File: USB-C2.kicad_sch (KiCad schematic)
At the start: 92 parts, among them J4 USB_C_Receptacle, J5 I2C2_PD_Controller, J6 I2C_Mux, J7 I2C_EEPROM, SW2 FW_Upgrade, U10 24LC256, U11 TPD4E02B04DQA, U12 TPD4E02B04DQA, U13 TPD4E02B04DQA, U14 TUSB1142IRNQR_C5216209, U8 TVS2200DRV, U9 TPS25762CQRQLRQ1

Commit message: Schematic reannotated
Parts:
- renumbered C31 to C32, C32 to C33, C33 to C34, C34 to C35, C35 to C36, C36 to C37, C37 to C38, C38 to C39, C39 to C40, C40 to C41, C41 to C42, C42 to C43, C43 to C44, C44 to C45, C45 to C46, C46 to C47, C47 to C48, C48 to C49, C49 to C50, C50 to C51, C51 to C52, C52 to C53, C53 to C54, C54 to C55, C55 to C56, C56 to C57, C57 to C58, C58 to C59, C59 to C60, C60 to C61, C61 to C62, C62 to C63, C63 to C64, C64 to C65, C65 to C66, C66 to C67, C67 to C68, C68 to C69, R12 to R21, R13 to R22, R14 to R23, R15 to R24, R16 to R25, R17 to R26, R18 to R27, R19 to R28, R20 to R29, R21 to R30, R22 to R31, R23 to R32, R24 to R33, R25 to R34, R51 to R35, R52 to R36, R47 to R37, R50 to R38, R26 to R39, R27 to R40, R28 to R41, R29 to R42, R96 to R43, R30 to R44, R31 to R45, R32 to R46, R33 to R47, R34 to R48, R35 to R49, R36 to R50, R37 to R51, R38 to R52, R39 to R53, R40 to R54, R41 to R55, R42 to R56, R43 to R57

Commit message: J11 changed to 8-pin PCIe connector, footprint assigned
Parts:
- J4: footprint Connector_USB:USB_C_Receptacle_Amphenol_12401610E4-2A -> SamacSys_Parts:USB420003A
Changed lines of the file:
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@@
 			)
 		)
-		(property "Footprint" "Connector_USB:USB_C_Receptacle_Amphenol_12401610E4-2A"
+		(property "Footprint" "SamacSys_Parts:USB420003A"
 			(at 374.65 48.26 0)
 			(effects

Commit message: footprints assigned, U21 change to SiRA80DP
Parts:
- TP3, TP4: footprint TestPoint:TestPoint_THTPad_1.5x1.5mm_Drill0.7mm -> TestPoint:TestPoint_Loop_D1.80mm_Drill1.0mm_Beaded
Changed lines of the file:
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@@
 			)
 		)
-		(property "Footprint" "TestPoint:TestPoint_THTPad_1.5x1.5mm_Drill0.7mm"
+		(property "Footprint" "TestPoint:TestPoint_Loop_D1.80mm_Drill1.0mm_Beaded"
 			(at 125.73 113.03 0)
 			(effects
@@
 			)
 		)
-		(property "Footprint" "TestPoint:TestPoint_THTPad_1.5x1.5mm_Drill0.7mm"
+		(property "Footprint" "TestPoint:TestPoint_Loop_D1.80mm_Drill1.0mm_Beaded"
 			(at 300.99 72.39 0)
 			(effects

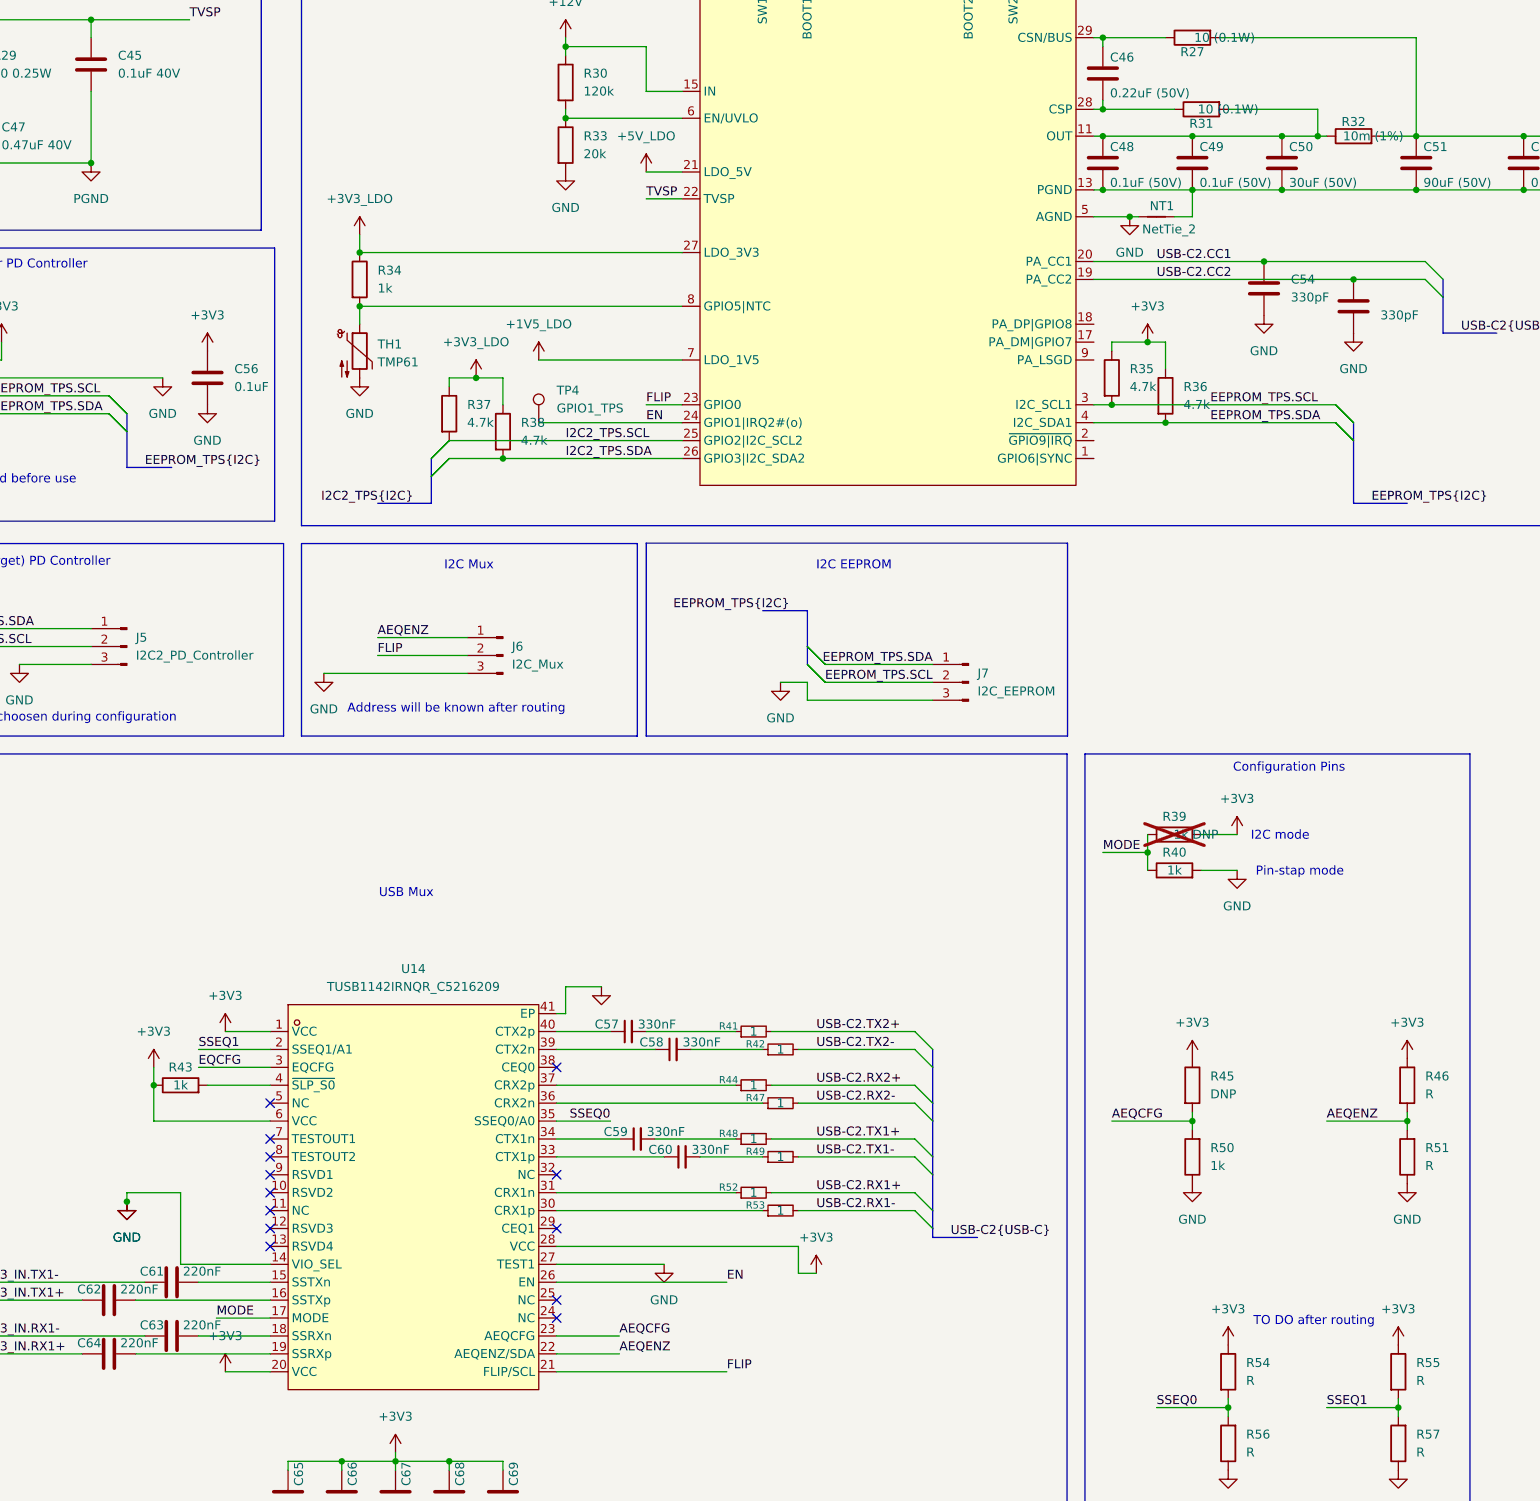
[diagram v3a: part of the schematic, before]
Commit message: Net class for USB SS signals created and applied on schematic
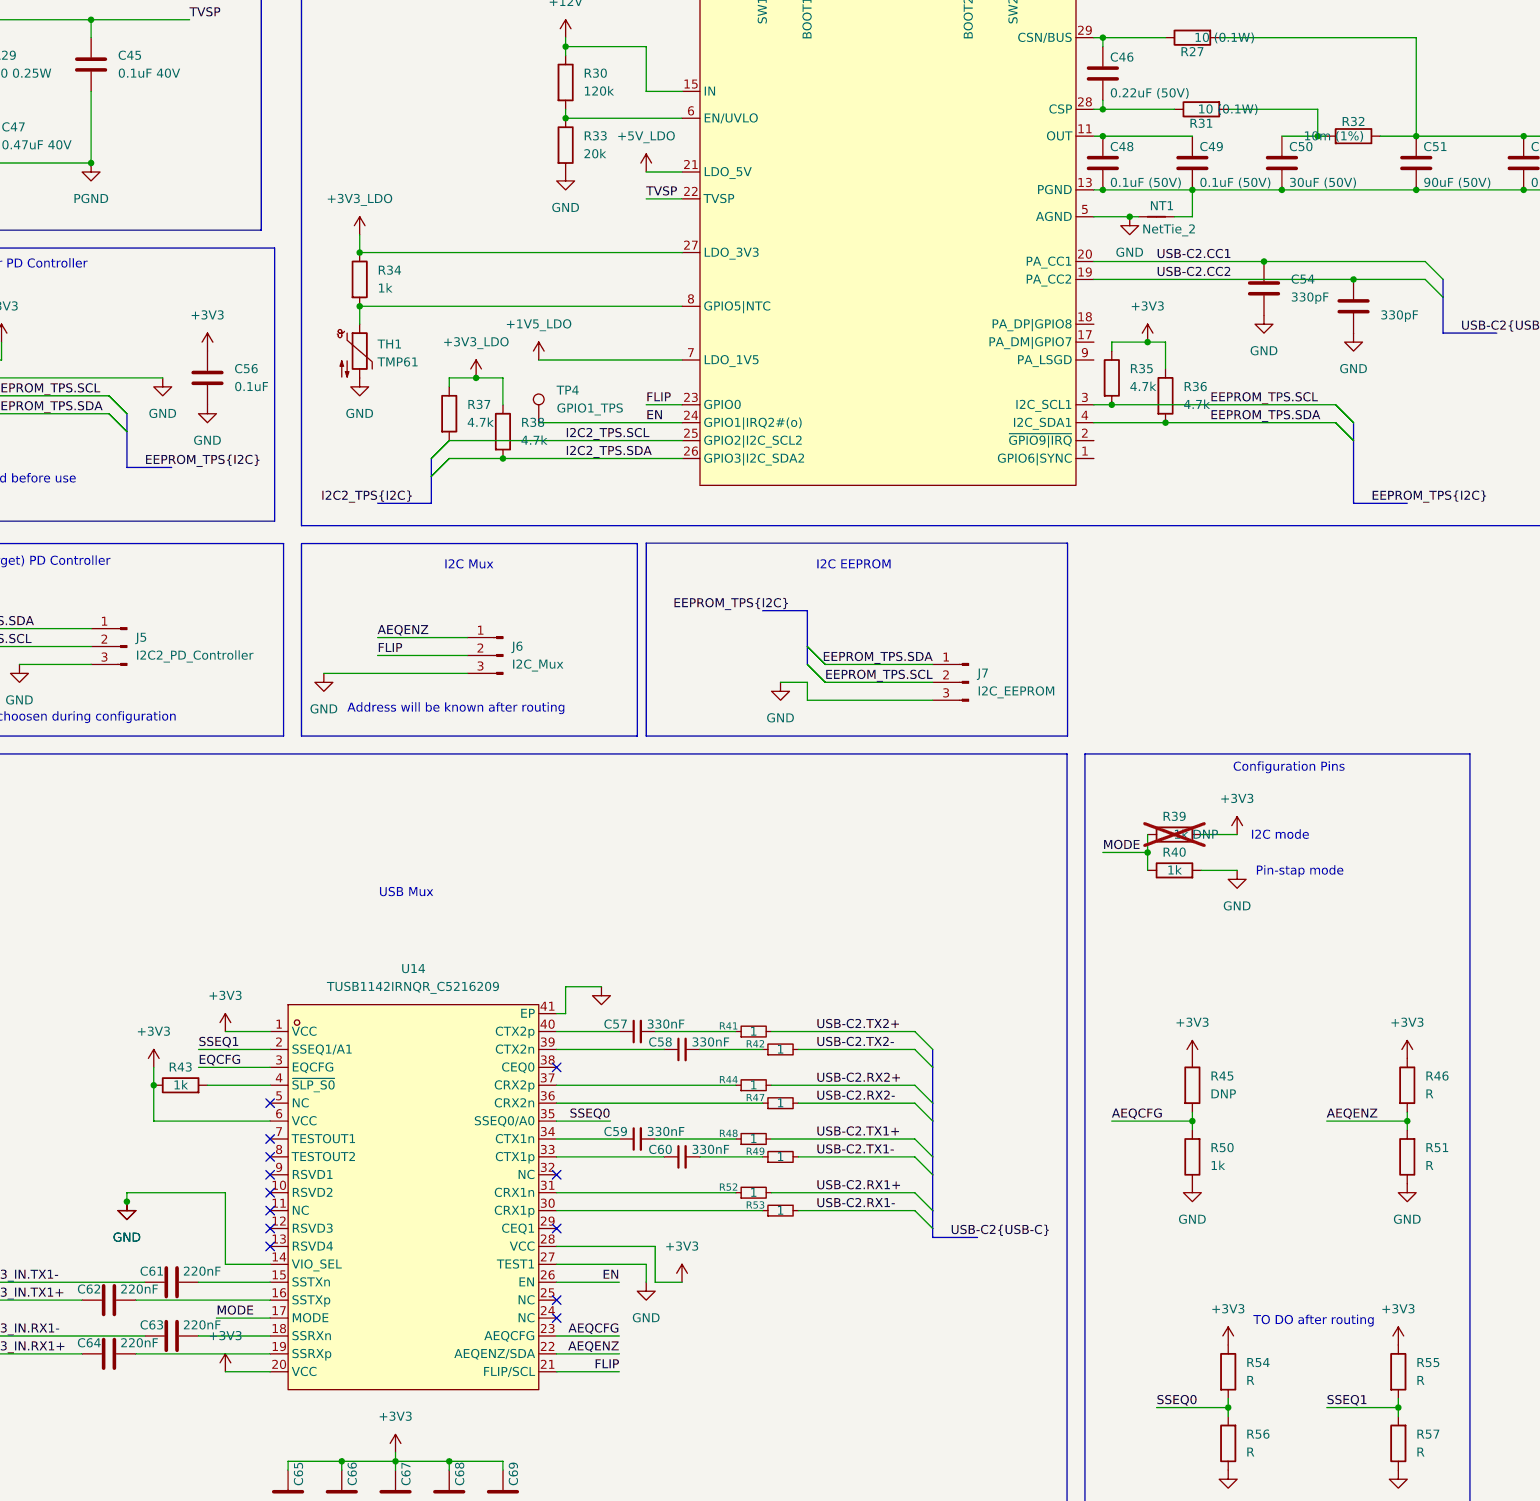
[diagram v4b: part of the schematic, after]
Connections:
- net VBUS: now also R32.1; no longer R32.2
- net at C48.1, C49.1, U9.11 (OUT): no longer C50.1, R31.2, R32.1
- new net: C50.1, R31.2, R32.2
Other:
- moved on the sheet: C57, C58, R32
